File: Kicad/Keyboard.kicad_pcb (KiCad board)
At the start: 2 copper layers, 161 parts, among them J1 USB_C_Receptacle_USB2.0_16P, J2 Conn_01x04, SW1 SW_Push, SW10 SW_Push, SW11 SW_Push, SW12 SW_Push, SW13 SW_Push, SW14 SW_Push, SW15 SW_Push, SW16 SW_Push, SW17 SW_Push, SW18 SW_Push, SW19 SW_Push, SW2 SW_Push, SW20 SW_Push, SW21 SW_Push, SW22 SW_Push, SW23 SW_Push, SW24 SW_Push, SW25 SW_Push, SW26 SW_Push, SW27 SW_Push, SW28 SW_Push, SW29 SW_Push, SW3 SW_Push, SW30 SW_Push, SW31 SW_Push, SW32 SW_Push, SW33 SW_Push, SW34 SW_Push, SW35 SW_Push, SW36 SW_Push, SW37 SW_Push, SW38 SW_Push, SW39 SW_Push, SW4 SW_Push, SW40 SW_Push, SW41 SW_Push, SW42 SW_Push, SW43 SW_Push, SW44 SW_Push, SW45 SW_Push, SW46 SW_Push, SW47 SW_Push, SW48 SW_Push, SW49 SW_Push, SW5 SW_Push, SW50 SW_Push, SW51 SW_Push, SW52 SW_Push, SW53 SW_Push, SW54 SW_Push, SW55 SW_Push, SW56 SW_Push, SW57 SW_Push, SW58 SW_Push, SW59 SW_Push, SW6 SW_Push, SW60 SW_Push, SW61 SW_Push, SW62 SW_Push, SW63 SW_Push, SW64 SW_Push, SW65 SW_Push, SW66 SW_Push, SW67 SW_Push, SW68 SW_Push, SW69 SW_Push, SW7 SW_Push, SW70 SW_Push, SW8 SW_Push, SW9 SW_Push, U1 ATmega32U4-A, U2 USB6B1, Y1 Crystal_GND24_Small

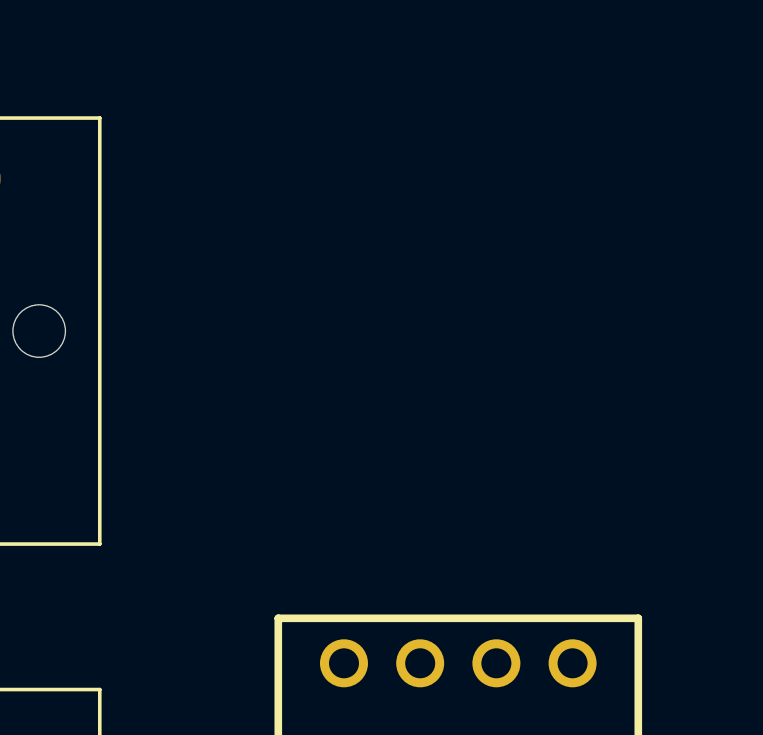
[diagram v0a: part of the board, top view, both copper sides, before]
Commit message: encoder layout + fix footprint
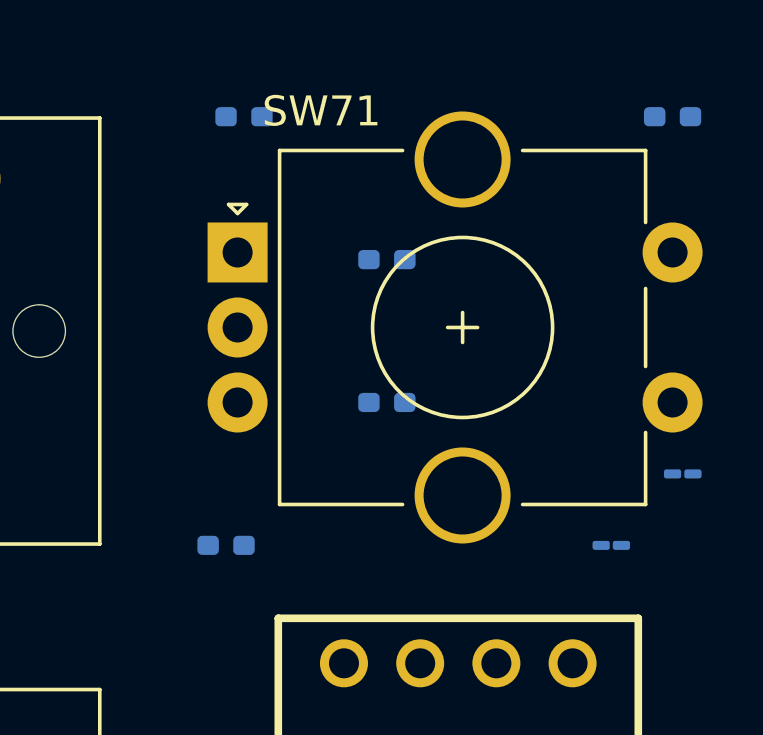
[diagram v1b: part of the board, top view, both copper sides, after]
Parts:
- added C8: 0.01uf, Capacitor_SMD:C_01005_0402Metric_Pad0.57x0.30mm_HandSolder, B.Cu at (348.0, 45.2)
- added C9: 0.01uf, Capacitor_SMD:C_01005_0402Metric_Pad0.57x0.30mm_HandSolder, B.Cu at (350.4, 42.9)
- added R5: 10k, Resistor_SMD:R_0402_1005Metric_Pad0.72x0.64mm_HandSolder, B.Cu at (350.0, 31.0)
- added R6: 10k, Resistor_SMD:R_0402_1005Metric_Pad0.72x0.64mm_HandSolder, B.Cu at (340.5, 35.7)
- added R7: 10k, Resistor_SMD:R_0402_1005Metric_Pad0.72x0.64mm_HandSolder, B.Cu at (340.5, 40.5)
- added R8: 10k, Resistor_SMD:R_0402_1005Metric_Pad0.72x0.64mm_HandSolder, B.Cu at (335.8, 31.0)
- added R9: 10k, Resistor_SMD:R_0402_1005Metric_Pad0.72x0.64mm_HandSolder, B.Cu at (335.2, 45.2)
- added SW71: RotaryEncoder_Switch, Rotary_Encoder:RotaryEncoder_Alps_EC11E-Switch_Vertical_H20mm_CircularMountingHoles, F.Cu at (335.5, 35.5)
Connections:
- U1 pad 37: unconnected-(U1-PF6-Pad37) -> Net-(U1-PF5)
- U1 pad 38: unconnected-(U1-PF5-Pad38) -> Net-(U1-PF5)

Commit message: cancer traces
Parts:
- added R10: 10k, Resistor_SMD:R_0402_1005Metric_Pad0.72x0.64mm_HandSolder, B.Cu at (74.1, 59.6)
- added SW72: SW_Push, Button_Switch_SMD:SW_Tactile_SPST_NO_Straight_CK_PTS636Sx25SMTRLFS, B.Cu at (69.0, 62.0)
- moved D67 302.4 mm to (333.4, 52.4)
- moved C4 1.75 mm to (49.2, 69.2)
- turned C8 to 0 degrees
- turned C9 to 0 degrees
- turned D51 to -90 degrees
- turned D66 to -90 degrees
- turned R3 to 0 degrees
- turned R4 to 0 degrees
- turned R8 to 0 degrees
- turned U2 to -90 degrees
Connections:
- C9 pad 1: Net-(U1-PF5) -> Net-(U1-PF6)
- R5 pad 1: Net-(R5-Pad1) -> Net-(U1-PF7)
- R7 pad 1: Net-(U1-PF5) -> Net-(U1-PF6)
- SW71 pad S2: Net-(R5-Pad1) -> Net-(U1-PF7)
- U1 pad 33: unconnected-(U1-~{HWB}/PE2-Pad33) -> Net-(U1-~{HWB}/PE2)
- U1 pad 36: unconnected-(U1-PF7-Pad36) -> Net-(U1-PF7)
- U1 pad 37: Net-(U1-PF5) -> Net-(U1-PF6)
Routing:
- net GND: track 0.00 -> 424.9 mm
- net C14: track 0.00 -> 361.8 mm
- net R4: track 0.00 -> 353.8 mm, vias 0 -> 2
- net R3: track 0.00 -> 336.0 mm
- net R0: track 0.00 -> 292.9 mm
- net R1: track 0.00 -> 266.3 mm
- net R2: track 0.00 -> 259.9 mm
- net C7: track 0.00 -> 219.3 mm, vias 0 -> 1
- net VBUS: track 0.00 -> 136.8 mm, vias 0 -> 2
- net C3: track 0.00 -> 115.4 mm
- net C11: track 0.00 -> 98.2 mm
- net C12: track 0.00 -> 93.1 mm
- net C10: track 0.00 -> 92.0 mm
- net C9: track 0.00 -> 92.0 mm
- net C8: track 0.00 -> 92.0 mm
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
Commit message: updated bootloader and reset footprints + symbols + reroute traces
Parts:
- SW1, SW72: value SW_Push -> ~; footprint Button_Switch_SMD:SW_Tactile_SPST_NO_Straight_CK_PTS636Sx25SMTRLFS -> a:Pushbuttonthing
- moved SW1 36.8 mm to (85.9, 63.9), turned to -90 degrees
- moved 10k1 32.0 mm to (73.3, 62.0)
- moved R2 11.1 mm to (49.1, 52.9)
- moved R1 10.9 mm to (51.2, 52.8), turned to -90 degrees
- moved SW72 9.35 mm to (78.2, 63.9), turned to 90 degrees
- moved R10 5.20 mm to (73.1, 64.7)
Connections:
- SW1 pad 2: Net-(U1-~{RESET}) -> unconnected-(SW1-Pad2)
- SW72 pad 1: Net-(U1-~{HWB}/PE2) -> unconnected-(SW72-Pad1)
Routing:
- net GND: track 424.9 -> 67.1 mm
- net C14: track 361.8 -> 84.1 mm
- net C7: track 219.3 -> 67.0 mm, vias 1 -> 0
- net R3: track 336.0 -> 272.4 mm
- net R4: track 353.8 -> 310.6 mm, vias 2 -> 0
- net VBUS: track 136.8 -> 97.2 mm
- net Net-(U1-D-): track 55.1 -> 19.1 mm
- net Net-(U1-D+): track 0.00 -> 17.1 mm, vias 0 -> 2
- net Net-(U1-~{HWB}/PE2): track 21.5 -> 4.79 mm
- net Net-(U1-XTAL2): track 17.9 -> 2.79 mm
- net D-: track 9.87 -> 2.29 mm
- net Net-(U1-XTAL1): track 10.8 -> 3.70 mm
- net C0: track 62.4 -> 57.5 mm
- net D+: track 0.00 -> 2.35 mm
- net Net-(U1-~{RESET}): track 15.6 -> 17.9 mm
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
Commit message: traces
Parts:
- moved C1 0.14 mm to (58.0, 71.5)
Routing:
- net SCL: track 0.00 -> 310.8 mm
- net SDA: track 0.00 -> 305.4 mm
- net C14: track 84.1 -> 360.9 mm, vias 0 -> 27
- net GND: track 67.1 -> 139.8 mm, vias 0 -> 4
- net R4: track 310.6 -> 351.7 mm, vias 0 -> 2
- net R2: track 259.9 -> 291.2 mm, vias 0 -> 2
- net C0: track 57.5 -> 88.0 mm, vias 0 -> 1
- net R1: track 266.3 -> 294.6 mm
- net R0: track 292.9 -> 321.0 mm, vias 0 -> 2
- net Net-(U1-XTAL2): track 2.79 -> 18.5 mm
- net VBUS: track 97.2 -> 106.4 mm, vias 2 -> 4
- net Net-(U1-XTAL1): track 3.70 -> 11.3 mm, vias 0 -> 2
- net Net-(U1-UCAP): track 0.00 -> 2.06 mm
- net Net-(U1-AREF): track 0.00 -> 1.75 mm

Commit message: routed all traces
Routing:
- net VBUS: track 106.4 -> 442.8 mm, vias 4 -> 12
- net Net-(U1-PF7): track 4.77 -> 333.1 mm, vias 0 -> 4
- net Net-(U1-PF6): track 12.7 -> 330.5 mm
- net Net-(U1-PF5): track 12.2 -> 328.5 mm, vias 0 -> 2
- net GND: track 139.8 -> 448.3 mm, vias 4 -> 7
- net C13: track 90.8 -> 347.2 mm, vias 0 -> 3
- net C12: track 93.1 -> 331.3 mm, vias 0 -> 3
- net C11: track 98.2 -> 325.5 mm, vias 0 -> 5
- net C10: track 92.0 -> 300.2 mm, vias 0 -> 3
- net C7: track 67.0 -> 236.7 mm, vias 0 -> 5
- net C9: track 92.0 -> 258.1 mm, vias 0 -> 1
- net C8: track 92.0 -> 243.7 mm
- net C6: track 67.0 -> 177.7 mm, vias 0 -> 3
- net C4: track 44.0 -> 141.6 mm, vias 0 -> 3
- net C5: track 67.0 -> 159.8 mm, vias 0 -> 3
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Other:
- board outline added: 324 x 97 mm

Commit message: added ground planes + fixed DRC errors/warnings
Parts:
- moved C9 1.39 mm to (349.0, 43.0)
- moved C8 1.24 mm to (348.0, 44.0)
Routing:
- net GND: track 448.3 -> 21.6 mm, vias 7 -> 0
- net VBUS: track 442.8 -> 437.6 mm, vias 12 -> 13
- net R0: track 320.4 -> 321.9 mm
- net C1: track 110.5 -> 111.7 mm
- net Net-(J1-D+-PadA6): track 12.6 -> 11.7 mm
- net Net-(U1-PF6): track 330.5 -> 329.9 mm
- net C9: track 258.1 -> 257.5 mm
- net Net-(U1-PF7): track 333.1 -> 333.7 mm
- net Net-(U1-XTAL2): track 18.5 -> 19.0 mm
- added copper zone on B.Cu, net GND
- added copper zone on F.Cu, net GND

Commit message: mounting holes
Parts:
- moved D66 1.46 mm to (314.3, 34.8)
- moved D9 1.29 mm to (71.4, 89.2)
- moved J1 0.23 mm to (49.6, 31.8)
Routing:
- net C2: track 149.7 -> 152.4 mm
- net C9: track 257.5 -> 255.9 mm
- net C13: track 347.2 -> 348.1 mm
- net C1: track 111.7 -> 112.5 mm
- net R1: track 293.8 -> 294.5 mm
- net Net-(J1-D+-PadA6): track 11.7 -> 12.4 mm
- net GND: track 21.6 -> 22.3 mm
- net R0: track 321.9 -> 321.3 mm, vias 2 -> 4
- net C8: track 243.7 -> 243.1 mm, vias 0 -> 3
- net Net-(D9-A): track 6.18 -> 6.75 mm
- net R3: track 329.0 -> 328.5 mm
- net VBUS: track 437.6 -> 437.1 mm, vias 13 -> 15
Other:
- outline, holes or cut-outs redrawn
- board text added: "Boot"
- board text added: "Keyboard v1.0 Designed by Darren Lin"
- board text added: "Reset"
